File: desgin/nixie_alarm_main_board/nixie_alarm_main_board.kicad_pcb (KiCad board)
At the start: 2 copper layers, 138.3 x 52.9 mm, 111 parts, among them IC1 LM3488MM, IC2 HV5530PG-G, IC3 TPS563219ADDFR, IC4 HV5530PG-G, IC6 CD40109BQNSRQ1, IC7 AP7363-33D-13, IC8 MCP4018T-502E_LT, J1 PJ-094H-SMT-TR, J2 JST XH 2.54 3 pin, J3 USB_C_Receptacle_USB2.0_16P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

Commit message: tvs protection try
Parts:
- added D1: ESD7551N2T5G, SamacSys_Parts:ESD7551N2T5G, F.Cu at (232.4, 82.3)
- added D3: ESD7551N2T5G, SamacSys_Parts:ESD7551N2T5G, F.Cu at (232.4, 86.0)
- added D4: PUSB3AB4Z, SamacSys_Parts:SON50P100X250X50-10N, F.Cu at (232.6, 89.3)
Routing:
- net USB_D-: track 36.6 -> 40.0 mm
- net USB_D+: track 38.5 -> 40.1 mm

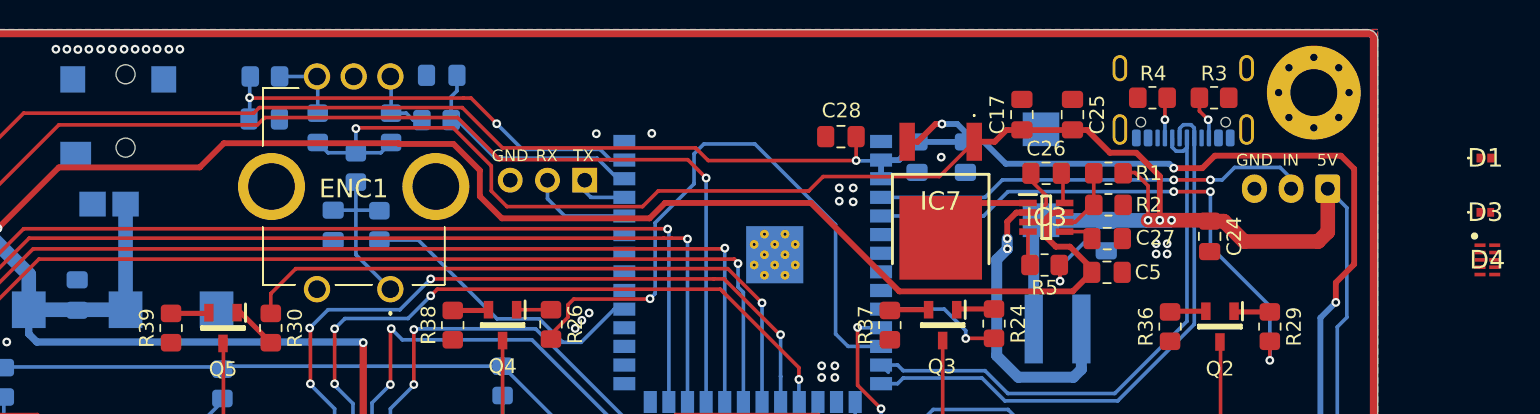
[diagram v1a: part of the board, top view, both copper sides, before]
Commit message: tvs added
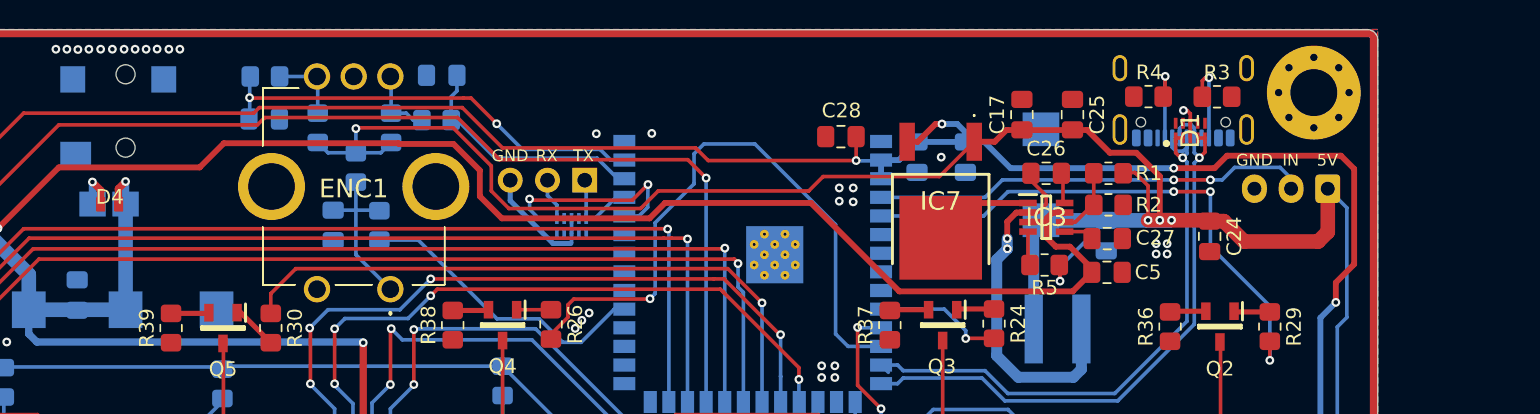
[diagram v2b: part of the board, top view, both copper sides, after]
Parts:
- D1: value ESD7551N2T5G -> PUSB3AB4Z; footprint SamacSys_Parts:ESD7551N2T5G -> SamacSys_Parts:SON50P100X250X50-10N
- D3: value ESD7551N2T5G -> PUSB3AB4Z; footprint SamacSys_Parts:ESD7551N2T5G -> SamacSys_Parts:SON50P100X250X50-10N; moved to B.Cu
- D4: value PUSB3AB4Z -> WE-TVS 824045812; footprint SamacSys_Parts:SON50P100X250X50-10N -> nixie:DFN-1610-2
- moved D4 94.0 mm to (138.7, 85.5)
- moved D3 62.3 mm to (170.2, 87.0), turned to -90 degrees
- moved D1 20.2 mm to (212.3, 80.5), turned to 90 degrees
- moved R4 0.28 mm to (209.5, 78.2)
- moved R3 0.21 mm to (214.2, 78.2)
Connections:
- D1 pad 1: GND -> USB_D-
- D3 pad 1: GND -> DEBUG_UART_RX
- D3 pad 2: USB_D+ -> unconnected-(D3-CH2-Pad2)
- D4 pad 1: unconnected-(D4-CH1-Pad1) -> GND
- D4 pad 2: unconnected-(D4-CH2-Pad2) -> +12V
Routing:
- net GND: track 35.7 -> 49.6 mm, vias 56 -> 58
- net DEBUG_UART_RX: track 6.99 -> 17.7 mm, vias 0 -> 2
- net +12V: track 324.0 -> 327.3 mm, vias 7 -> 8
- net Net-(J3-CC1): track 2.80 -> 5.64 mm
- net Net-(J3-CC2): track 3.01 -> 5.73 mm
- net USB_D-: track 40.0 -> 42.4 mm, vias 0 -> 1
- net USB_D+: track 40.1 -> 42.4 mm, vias 0 -> 1
- net DEBUG_UART_TX: track 3.63 -> 5.85 mm

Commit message: fixes added
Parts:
- removed 12V, 3.3V, 5V, HV: TestPoint_Pad_D1.5mm, TestPoint:TestPoint_Pad_D1.5mm
- removed the GND at (111.0, 120.2)
- removed REF** (x4): MountingHole_3.2mm_M3_Pad_Via, MountingHole:MountingHole_3.2mm_M3_Pad_Via
- added +12V: +12V, TestPoint:TestPoint_Pad_D2.0mm, F.Cu at (104.0, 120.3)
- added +3.3V: +3.3V, TestPoint:TestPoint_Pad_D2.0mm, F.Cu at (96.8, 120.2)
- added +5V: +5V, TestPoint:TestPoint_Pad_D2.0mm, F.Cu at (100.5, 120.3)
- added +HV: +HV, TestPoint:TestPoint_Pad_D2.0mm, F.Cu at (107.5, 120.3)
- added D5: CDBUR0520, Diode_SMD:D_0603_1608Metric_Pad1.05x0.95mm_HandSolder, F.Cu at (90.2, 93.1)
- added GND: GND, TestPoint:TestPoint_Pad_D2.0mm, F.Cu at (111.0, 120.3)
- added H1: MountingHole_Pad, MountingHole:MountingHole_3.2mm_M3_Pad_Via, F.Cu at (91.0, 77.8)
- added H2: MountingHole_Pad, MountingHole:MountingHole_3.2mm_M3_Pad_Via, F.Cu at (220.8, 77.8)
- added H3: MountingHole_Pad, MountingHole:MountingHole_3.2mm_M3_Pad_Via, F.Cu at (91.2, 122.4)
- added H4: MountingHole_Pad, MountingHole:MountingHole_3.2mm_M3_Pad_Via, F.Cu at (220.9, 122.3)
- added R6: 470Ω, Resistor_SMD:R_0805_2012Metric_Pad1.20x1.40mm_HandSolder, F.Cu at (217.2, 87.6)
- D1: moved to B.Cu
- J5: value Goldpin 3pin -> Goldpin 3pin
- R5: value 100kΩ -> 0Ω
- moved R5 107.2 mm to (95.5, 81.3), turned to 180 degrees
- moved C24 8.05 mm to (221.7, 87.7)
- moved C5 4.16 mm to (202.5, 90.0)
- moved D1 3.53 mm to (212.3, 84.0), turned to -90 degrees
- moved R12 1.85 mm to (96.5, 76.8)
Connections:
- C2 pad 1: HV -> Net-(D2-K)
- ENC1 pad MH1: (no net) -> GND
- ENC1 pad MH2: (no net) -> GND
- J1 pad MP1: unconnected-(J1-PadMP1) -> GND
- J1 pad MP2: unconnected-(J1-PadMP2) -> GND
- J2 pad 2: LED_DATA -> Net-(J2-Pin_2)
- LS1 pad 2: Net-(LS1--) -> Net-(D5-A)
- R12 pad 1: HV -> Net-(D2-K)
- R36 pad 1: GND -> Net-(Q2-D)
- R36 pad 2: Net-(Q2-S) -> Net-(N1-Padic)
- R37 pad 1: GND -> Net-(Q3-D)
- R37 pad 2: Net-(Q3-S) -> Net-(N2-Padic)
- R38 pad 1: GND -> Net-(Q4-D)
- R38 pad 2: Net-(Q4-S) -> Net-(N3-Padic)
- R39 pad 1: GND -> Net-(Q5-D)
- R39 pad 2: Net-(Q5-S) -> Net-(N4-Padic)
- R40 pad 1: GND -> Net-(Q6-D)
- R40 pad 2: Net-(Q6-S) -> Net-(N5-Padic)
- R41 pad 1: GND -> Net-(Q7-D)
- R41 pad 2: Net-(Q7-S) -> Net-(N6-Padic)
- R5 pad 1: Net-(IC3-PG) -> Net-(D2-K)
- R5 pad 2: +5V -> HV
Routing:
- net (no net): track 801.8 -> 0.00 mm
- net +12V: track 327.3 -> 315.9 mm, vias 8 -> 12
- net HV: track 229.7 -> 222.6 mm
- net Net-(D5-A): track 0.00 -> 6.32 mm
- net Net-(D2-K): track 0.00 -> 5.67 mm
- net Net-(J2-Pin_2): track 0.00 -> 4.28 mm
- net Net-(D2-A): track 15.0 -> 11.0 mm
- net +5V: track 273.4 -> 269.6 mm, vias 6 -> 5
- net Net-(IC3-PG): track 1.98 -> 0.00 mm
- net USB_D-: track 42.4 -> 41.1 mm, vias 1 -> 0
- net Net-(IC2-~{LE}): track 68.8 -> 69.6 mm
- net NX_DOT_6: track 101.7 -> 102.4 mm
- net USB_D+: track 42.4 -> 41.9 mm, vias 1 -> 0
- net GND: track 49.6 -> 49.4 mm, vias 58 -> 152
- net LED_DATA: track 29.9 -> 29.7 mm, vias 2 -> 1

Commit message: final fixes
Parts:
- moved C12 0.28 mm to (97.5, 90.2)
- moved R10 0.07 mm to (92.7, 89.9)
- turned R36 to -90 degrees
- turned R37 to -90 degrees
- turned R38 to -90 degrees
- turned R39 to -90 degrees
- turned R40 to -90 degrees
- turned R41 to -90 degrees
- renumbered +12V to +12V1, +3.3V to +3.3V1, +5V to +5V1, +HV to +HV1, GND to GND1
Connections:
- D2 pad 1: HV -> Net-(D2-K)
- IC3 pad 4: Net-(IC3-PG) -> unconnected-(IC3-PG-Pad4)
- N1 pad ic: Net-(Q2-D) -> Net-(N1-Padic)
- N2 pad ic: Net-(Q3-D) -> Net-(N2-Padic)
- N3 pad ic: Net-(Q4-D) -> Net-(N3-Padic)
- N4 pad ic: Net-(Q5-D) -> Net-(N4-Padic)
- N5 pad ic: Net-(Q6-D) -> Net-(N5-Padic)
- N6 pad ic: Net-(Q7-D) -> Net-(N6-Padic)
- Q1 pad 3: Net-(LS1--) -> Net-(D5-A)
- Q2 pad 2: Net-(Q2-S) -> GND
- Q3 pad 2: Net-(Q3-S) -> GND
- Q4 pad 2: Net-(Q4-S) -> GND
- Q5 pad 2: Net-(Q5-S) -> GND
- Q6 pad 2: Net-(Q6-S) -> GND
- Q7 pad 2: Net-(Q7-S) -> GND
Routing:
- net GND: track 49.4 -> 96.7 mm, vias 152 -> 245
- net HV: track 222.6 -> 193.6 mm, vias 3 -> 2
- net Net-(D2-K): track 5.67 -> 34.3 mm, vias 0 -> 1
- net NX_DOT_3: track 43.0 -> 26.4 mm
- net Net-(N6-Padic): track 0.00 -> 15.0 mm
- net Net-(N5-Padic): track 0.00 -> 14.6 mm
- net Net-(N3-Padic): track 0.00 -> 14.5 mm
- net Net-(N2-Padic): track 0.00 -> 14.5 mm
- net Net-(N1-Padic): track 0.00 -> 14.4 mm
- net Net-(N4-Padic): track 0.00 -> 14.4 mm
- net Net-(Q4-D): track 13.0 -> 4.32 mm
- net Net-(Q5-D): track 13.0 -> 4.39 mm
- net Net-(Q3-D): track 13.0 -> 4.52 mm
- net Net-(Q7-D): track 12.8 -> 4.32 mm
- net Net-(Q2-D): track 12.8 -> 4.39 mm
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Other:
- board text added: "+12V"
- board text added: "+3.3V"
- board text added: "+5V"
- board text added: "+HV"

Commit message: little adujstments
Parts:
- moved R11 1.25 mm to (96.6, 79.0)
- moved Q1 0.15 mm to (90.9, 95.7)
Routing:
- net HV: track 193.6 -> 197.1 mm
- net Net-(IC8-A): track 7.31 -> 8.64 mm
- net +12V: track 315.7 -> 316.9 mm
- net Net-(IC1-FB): track 18.9 -> 19.9 mm
- net USB_D-: track 41.1 -> 40.6 mm
- net USB_D+: track 41.9 -> 41.4 mm
- net GND: vias 245 -> 247

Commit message: new border
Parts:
- moved H3 0.20 mm to (91.0, 122.4)
- moved H2 0.16 mm to (220.9, 77.8)
- moved H4 0.11 mm to (220.9, 122.4)
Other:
- outline, holes or cut-outs redrawn

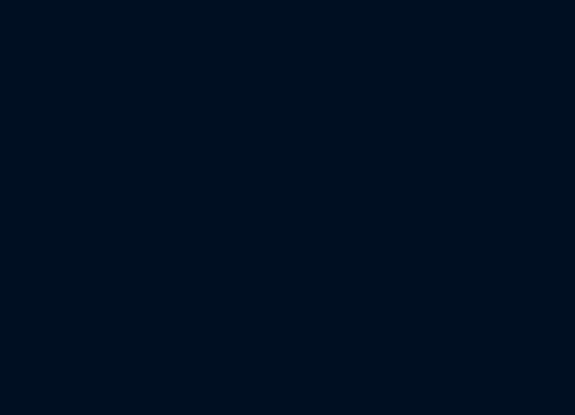
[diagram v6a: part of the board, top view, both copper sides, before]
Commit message: dc plug module describe
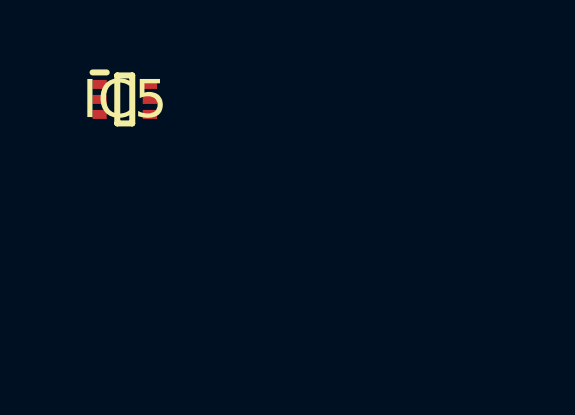
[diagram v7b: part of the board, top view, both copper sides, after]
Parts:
- added IC5: AP62250Z6-7, SamacSys_Parts:SOTFL50P160X60-6N, F.Cu at (1.25, 1.02)
